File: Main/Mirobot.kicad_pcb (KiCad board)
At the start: 2 copper layers, 110 x 31.5 mm, 45 parts, among them M1 ESP8266-ESP-12, P2 RIGHT_STEPPER, P3 LEFT_STEPPER, Q1 S8050, Q2 S8050, SW1 LEFT_BUMP, SW2 RIGHT_BUMP, SW3 POWER_SWITCH, U1 phototransistor, U2 phototransistor, U3 PCF8591, U4 74HC595, U5 ULN2803A, U6 USB-A-PLUG, U7 CH340G, U8 LD1117S33CTR, X1 12MHz

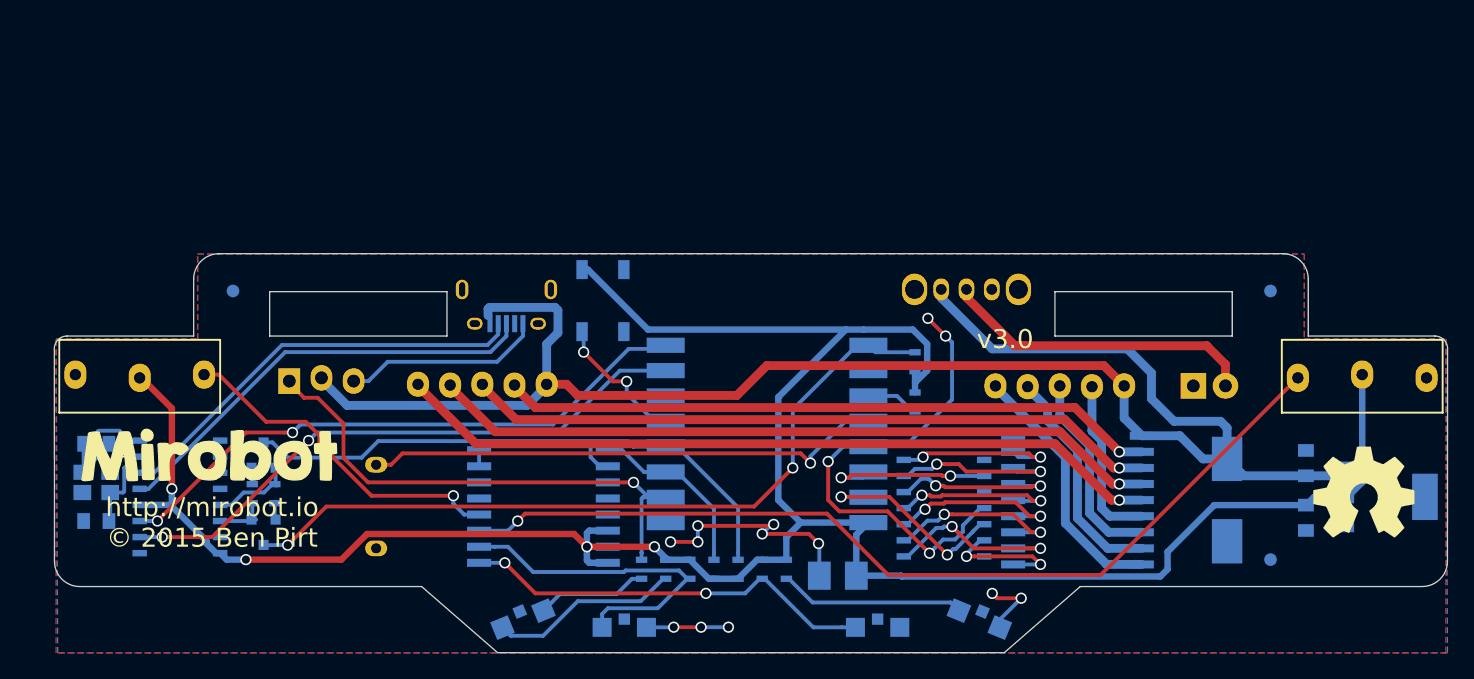
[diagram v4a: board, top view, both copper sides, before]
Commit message: Update the BoM to embed it into KiCad
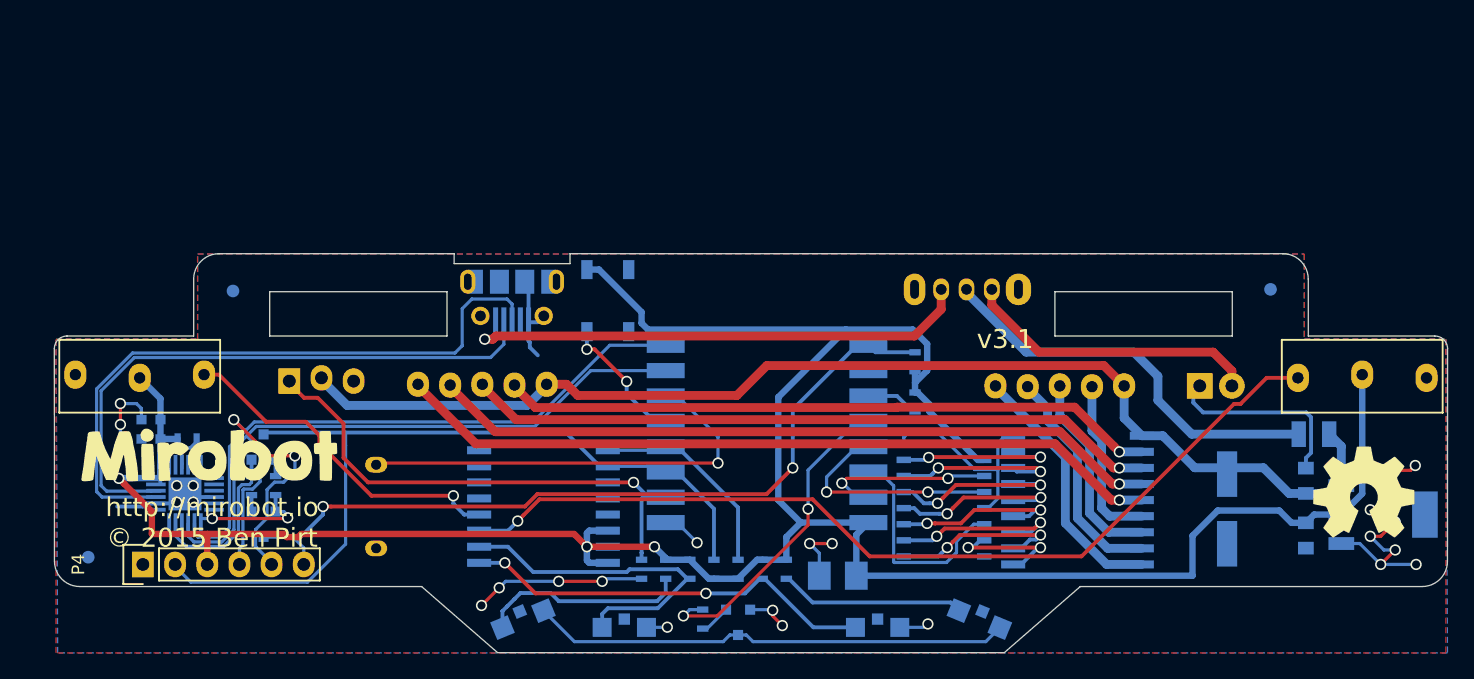
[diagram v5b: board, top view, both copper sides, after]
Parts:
- removed C2: 22pF, Capacitors_SMD:C_0805
- removed U7: CH340G, SMD_Packages:SO-16-N
- removed X1: 12MHz, Crystals:crystal_FA238-TSX3225
- added C4: 4.7uF, Capacitors_SMD:C_0603, B.Cu at (121.5, 135.1)
- added F1: FUSE, Fuse_Holders_and_Fuses:Fuse_SMD1206_Reflow, B.Cu at (213.4, 134.7)
- added P1: USB_OTG, Custom:MOLEX_MICRO_USB, B.Cu at (150.1, 125.4)
- added P4: CONN_01X06, Pin_Headers:Pin_Header_Straight_1x06, F.Cu at (120.9, 145.0)
- added Q3: S8050, Custom:SOT-23, B.Cu at (167.9, 149.6)
- added R12: 10k, Resistors_SMD:R_0603, B.Cu at (129.5, 138.8)
- added R13: 10k, Resistors_SMD:R_0603, B.Cu at (165.1, 149.4)
- ART1: footprint Mirobot:MIROBOT_LOGO -> Custom:MIROBOT_LOGO
- ART2: footprint Mirobot:OSHW_LOGO -> Custom:OSHW_LOGO
- C1: value 22pF -> 470uF; footprint Capacitors_SMD:C_0805 -> Capacitors_SMD:c_elec_6.3x7.7
- C3: value 470uF -> 0.1uF; footprint Capacitors_SMD:c_elec_8x10 -> Capacitors_SMD:C_0603
- D1, D2: footprint Mirobot:SIDE-LED-REVERSED -> Custom:SIDE-LED-REVERSED
- FID1, FID2, FID3: footprint Mirobot:Fiducial -> Custom:Fiducial; moved to B.Cu
- L1: footprint Mirobot:WS2812B -> Custom:WS2812B
- M1: footprint Mirobot:ESP-07 -> Custom:ESP-07
- P2, P3: footprint Mirobot:JST_XH-1x05 -> Custom:JST_XH-1x05
- PEN1: footprint Mirobot:Pin_Header_Staggered_1x03 -> Custom:Pin_Header_Staggered_1x03
- Q1, Q2: footprint TO_SOT_Packages_SMD:SOT-23 -> Custom:SOT-23
- R10: value 10k -> 10K
- SG1: footprint Mirobot:BUZZER -> Custom:BUZZER
- SW1, SW2: footprint Mirobot:LEVER_SWITCH -> Custom:LEVER_SWITCH
- SW3: footprint Mirobot:SMALL_SLIDE_SWITCH -> Custom:SMALL_SLIDE_SWITCH
- U1, U2: footprint Mirobot:SIDE-LED -> Custom:SIDE-LED
- U5: footprint Mirobot:SO-18 -> Custom:SO-18
- U6: value USB-A-PLUG -> CP2104; footprint Connect:USB_Micro-B -> Custom:QFN-24-1EP_4x4mm_Pitch0.5mm-easySolder
- moved FID3 93.3 mm to (116.6, 144.5)
- moved C1 89.3 mm to (206.5, 140.7), turned to 90 degrees
- moved C3 85.2 mm to (121.5, 133.6), turned to 180 degrees
- moved U6 29.5 mm to (124.2, 139.5)
- moved R10 6.72 mm to (124.4, 135.1), turned to 0 degrees
- moved C6 1.40 mm to (212.7, 138.4)
- moved U8 1.40 mm to (218.8, 141.1)
- moved C8 1.40 mm to (212.7, 142.7)
- moved R11 0.64 mm to (131.4, 138.8), turned to 90 degrees
- moved Q1 0.63 mm to (130.4, 135.8)
- moved Q2 0.63 mm to (130.4, 141.9)
- moved BATT1 0.51 mm to (205.6, 130.9)
- moved L1 0.38 mm to (157.6, 124.2)
- turned SW3 to 0 degrees
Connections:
- C1 pad 1: Net-(C1-Pad1) -> VSS
- C3 pad 1: VSS -> +3V3
- D1 pad 1: GND -> Net-(D1-Pad1)
- D2 pad 1: GND -> Net-(D1-Pad1)
- M1 pad 11: SDA -> SCL
- M1 pad 12: SCL -> SDA
- M1 pad 14: GPIO5 -> BUZZER
- M1 pad 4: BUZZER -> LED_EN
- R10 pad 1: Net-(Q2-Pad1) -> +3V3
- R10 pad 2: Net-(Q1-Pad2) -> Net-(R10-Pad2)
- R11 pad 1: Net-(Q1-Pad1) -> Net-(Q2-Pad1)
- R11 pad 2: Net-(Q2-Pad2) -> Net-(Q1-Pad2)
- R4 pad 2: SCL -> SDA
- R5 pad 2: SDA -> SCL
- SW3 pad 1: VSS -> Net-(BATT1-Pad2)
- SW3 pad 2: Net-(BATT1-Pad2) -> Net-(F1-Pad1)
- SW3 pad 3: Net-(SW3-Pad3) -> +5V
- SW3 pad 4: (no net) -> GND
- U4 pad 11: SR_DATA -> SR_CLK
- U4 pad 14: SR_CLK -> SR_DATA
- U6 pad 1: VSS -> Net-(U6-Pad1)
- U6 pad 2: Net-(U6-Pad2) -> GND
- U6 pad 5: GND -> +3V3
- U6 pad 6: (no net) -> +3V3
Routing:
- net Net-(P1-Pad2): track 0.00 -> 47.4 mm
- net +5V: track 0.00 -> 41.1 mm, vias 0 -> 1
- net Net-(D1-Pad1): track 0.00 -> 38.6 mm
- net VSS: track 132.6 -> 94.3 mm
- net Net-(U6-Pad2): track 33.7 -> 0.00 mm
- net Net-(F1-Pad1): track 0.00 -> 32.2 mm
- net LED_EN: track 0.00 -> 25.2 mm, vias 0 -> 2
- net GND: track 85.8 -> 105.3 mm, vias 15 -> 27
- net TXD: track 47.3 -> 66.7 mm
- net SCL: track 47.8 -> 66.3 mm
- net +3V3: track 191.6 -> 210.0 mm, vias 4 -> 3
- net Net-(P1-Pad3): track 34.9 -> 52.4 mm
- net RXD: track 47.9 -> 60.8 mm, vias 2 -> 0
- net SR_LATCH: track 6.71 -> 17.9 mm, vias 1 -> 2
- net Net-(C2-Pad1): track 10.1 -> 0.00 mm
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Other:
- outline, holes or cut-outs redrawn
- net class Default: clearance 0.254 -> 0.1; trace_width 0.3048 -> 0.254
- rule trace_clearance: 0.254 -> 0.1
- rule trace_min: 0.254 -> 0.2
- board text added: "USB"
- board text added: "v3.1"
- board text removed: "OFF"
- board text removed: "ON"
- board text removed: "v3.0"
